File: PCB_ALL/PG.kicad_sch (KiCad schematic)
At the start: 25 parts, among them SW1 SW_SP3T, U4 NE555P

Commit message: Updated KiCAD project files
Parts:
- removed BT1: Battery_Cell, symbol Device:Battery_Cell
- removed SW1: SW_SP3T, symbol Switch:SW_SP3T
- added Ammeter+2, Ammeter+3, Ammeter-2, Ammeter-3, CAP3, CAP4, CAP5, CAP6, PWR+1, PWR-1, VBB3, VBB4, VBE+1, VBE-1, VCE+1, VCE-1, VDD1, VDD2, Vcc1, Vcc2, Vgg+2, Vgg-2: Conn_01x01, Connector_PinHeader_2.54mm:PinHeader_1x01_P2.54mm_Vertical, symbol Connector_Generic:Conn_01x01
- added Q4: NPN, symbol Simulation_SPICE:NPN
- added Q5: NMOS, symbol Simulation_SPICE:NMOS
- added R17, R18: R, symbol Device:R
- added R19: 100k, symbol Device:R
- added R20: 1k, symbol Device:R
- C5, C6, C7, C8: footprint (none) -> Capacitor_THT:C_Disc_D3.0mm_W2.0mm_P2.50mm
- CRO1, CRO2, SG1, SG2: footprint (none) -> Connector_PinHeader_2.54mm:PinHeader_1x01_P2.54mm_Vertical
- CRO3, CRO4: renamed from CRO; footprint (none) -> Connector_PinHeader_2.54mm:PinHeader_1x01_P2.54mm_Vertical
- D3: footprint (none) -> LED_THT:LED_D3.0mm
- D4: footprint (none) -> Diode_THT:D_A-405_P7.62mm_Horizontal
- L1: footprint (none) -> Inductor_THT:L_Axial_L5.3mm_D2.2mm_P7.62mm_Horizontal_Vishay_IM-1
- R13, R14, R15, R16, RV1: footprint (none) -> Resistor_THT:R_Axial_DIN0207_L6.3mm_D2.5mm_P7.62mm_Horizontal
- SG-1: renamed from SG-; footprint (none) -> Connector_PinHeader_2.54mm:PinHeader_1x01_P2.54mm_Vertical
- SQ+1: renamed from SQ+; footprint (none) -> Connector_PinHeader_2.54mm:PinHeader_1x01_P2.54mm_Vertical
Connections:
- net GND: now also Q5.3 (S), VDD2.1 (Pin_1), Vgg+2.1 (Pin_1)
- net at C7.1: now also CAP6.1 (Pin_1)
- net at CRO3.1 (Pin_1), L1.2: now also CAP3.1 (Pin_1)
- net at SQ+1.1 (Pin_1): now also PWR+1.1 (Pin_1)
- net at D4.2 (A): now also PWR-1.1 (Pin_1)
- net at C6.1: now also CAP5.1 (Pin_1)
- net at C5.1: now also CAP4.1 (Pin_1)
- new net: Q4.3 (E), VBB4.1 (Pin_1), VBE-1.1 (Pin_1), VCE-1.1 (Pin_1), Vcc2.1 (Pin_1)
- new net: Ammeter-2.1 (Pin_1), R17.2, VBE+1.1 (Pin_1)
- new net: R18.2, Vcc1.1 (Pin_1)
- new net: R20.2, VDD1.1 (Pin_1)
- new net: Ammeter+3.1 (Pin_1), R18.1, VCE+1.1 (Pin_1)
- new net: Q5.1 (D), R20.1
- new net: Q5.2 (G), R19.2
- new net: Ammeter-3.1 (Pin_1), Q4.1 (C)
- new net: Ammeter+2.1 (Pin_1), Q4.2 (B)
- new net: R19.1, Vgg-2.1 (Pin_1)
- new net: R17.1, VBB3.1 (Pin_1)
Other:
- note added: "CE"
- note added: "NMOS O/P and TRANSFER CHAR."
- note added: "To Do - PLL 565 Barrier Capacitance Delayed Linear Sweep"
- note removed: "To Do - PLL 565 Barrier Capacitance"
- moved on the sheet: C5, C6, C7, L1, R13

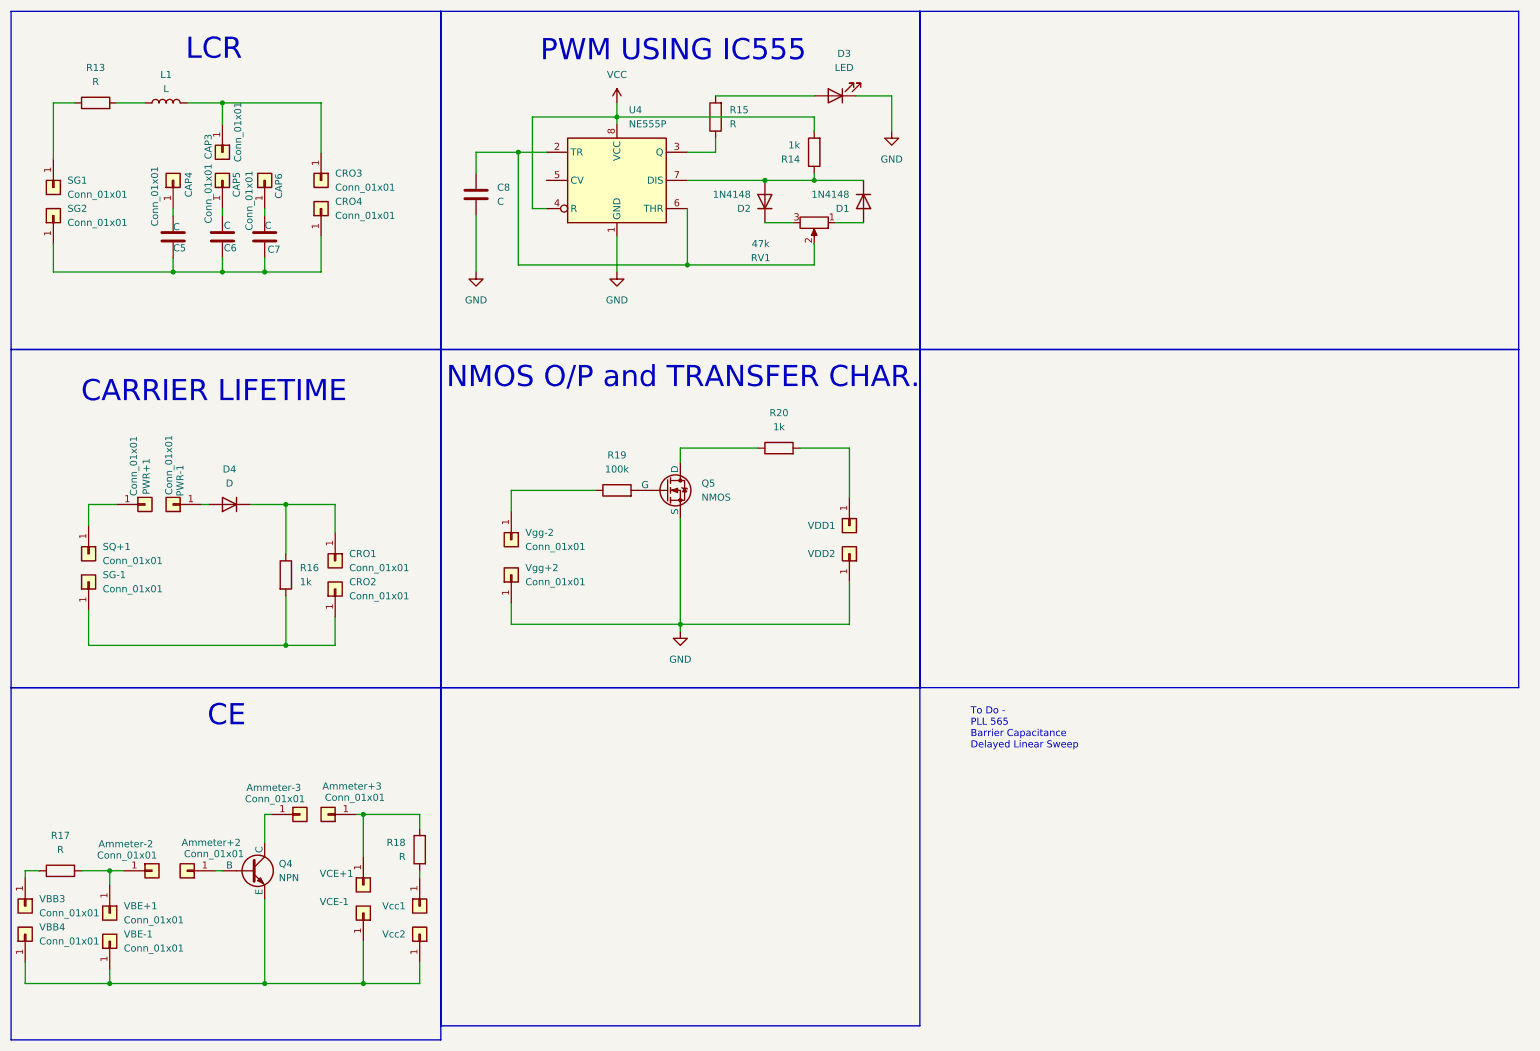
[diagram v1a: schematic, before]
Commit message: Updated KiCAD schematic and PCB layout
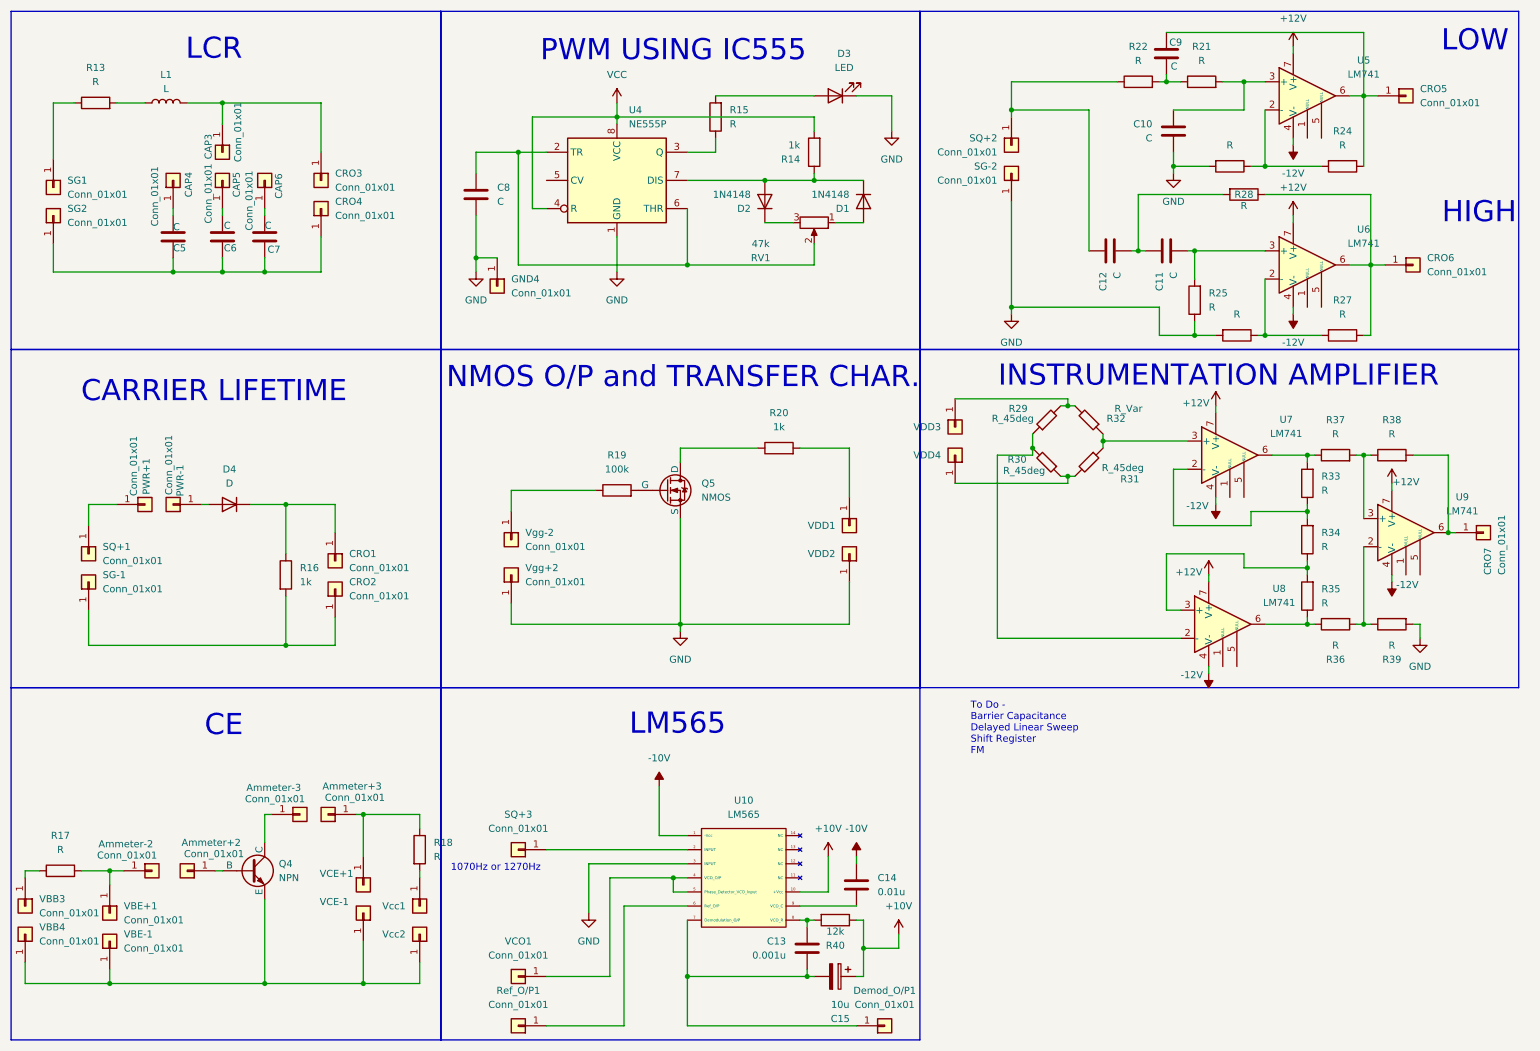
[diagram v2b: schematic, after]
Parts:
- added C10, C11, C12, C9: C, Capacitor_SMD:C_0805_2012Metric_Pad1.18x1.45mm_HandSolder, symbol Device:C
- added C13: 0.001u, Capacitor_SMD:C_0805_2012Metric_Pad1.18x1.45mm_HandSolder, symbol Device:C
- added C14: 0.01u, Capacitor_SMD:C_0805_2012Metric_Pad1.18x1.45mm_HandSolder, symbol Device:C
- added C15: 10u, Capacitor_THT:CP_Radial_D5.0mm_P2.50mm, symbol Device:C_Polarized
- added CRO5, CRO6, CRO7, Demod_O/P1, GND4, SG-2, SQ+2, SQ+3, VCO1, VDD3, VDD4: Conn_01x01, Connector_PinSocket_2.54mm:PinSocket_1x01_P2.54mm_Vertical, symbol Connector_Generic:Conn_01x01
- added R21, R22, R23, R24, R25, R26, R27, R28, R33, R34, R35, R36, R37, R38, R39: R, Resistor_SMD:R_0805_2012Metric_Pad1.20x1.40mm_HandSolder, symbol Device:R
- added R29, R30, R31: R_45deg, Resistor_SMD:R_0805_2012Metric_Pad1.20x1.40mm_HandSolder, symbol Device:R_45deg
- added R32: R_Var, Connector_PinSocket_2.54mm:PinSocket_2x01_P2.54mm_Vertical, symbol Device:R_45deg
- added R40: 12k, Resistor_SMD:R_0805_2012Metric_Pad1.20x1.40mm_HandSolder, symbol Device:R
- added Ref_O/P1: Conn_01x01, Connector_PinHeader_2.54mm:PinHeader_1x01_P2.54mm_Vertical, symbol Connector_Generic:Conn_01x01
- added U10: LM565, Package_DIP:CERDIP-14_W7.62mm_SideBrazed_LongPads, symbol W25Q64BVSSIG:LM565
- added U5, U6, U7, U8, U9: LM741, Package_SO:SOIC-8_3.9x4.9mm_P1.27mm, symbol Amplifier_Operational:LM741
- Ammeter+2, Ammeter+3, Ammeter-2, Ammeter-3, CAP3, CAP4, CAP5, CAP6, CRO1, CRO2, CRO3, CRO4, PWR+1, PWR-1, SG-1, SG1, SG2, SQ+1, VBB3, VBB4, VBE+1, VBE-1, VCE+1, VCE-1, VDD1, VDD2, Vcc1, Vcc2, Vgg+2, Vgg-2: footprint Connector_PinHeader_2.54mm:PinHeader_1x01_P2.54mm_Vertical -> Connector_PinSocket_2.54mm:PinSocket_1x01_P2.54mm_Vertical
- C5, C6, C7, C8: footprint Capacitor_THT:C_Disc_D3.0mm_W2.0mm_P2.50mm -> Capacitor_SMD:C_0805_2012Metric_Pad1.18x1.45mm_HandSolder
- Q4, Q5: footprint (none) -> Package_TO_SOT_SMD:SOT-23
- R13, R14, R15, R16: footprint Resistor_THT:R_Axial_DIN0207_L6.3mm_D2.5mm_P7.62mm_Horizontal -> Resistor_SMD:R_0805_2012Metric_Pad1.20x1.40mm_HandSolder
- R17, R18, R19, R20: footprint (none) -> Resistor_SMD:R_0805_2012Metric_Pad1.20x1.40mm_HandSolder
- RV1: footprint Resistor_THT:R_Axial_DIN0207_L6.3mm_D2.5mm_P7.62mm_Horizontal -> Potentiometer_THT:Potentiometer_Bourns_3296P_Horizontal
- U4: footprint Package_DIP:DIP-8_W7.62mm -> Package_SO:SOIC-8_3.9x4.9mm_P1.27mm
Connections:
- net GND: now also C10.2, GND4.1 (Pin_1), R23.2, R25.1, R26.2, R39.2, SG-2.1 (Pin_1), U10.3 (INPUT)
- new net: R37.2, R38.1, U9.3 (+)
- new net: CRO7.1 (Pin_1), R38.2, U9.6
- new net: C12.1, R22.1, SQ+2.1 (Pin_1)
- new net: C11.1, C12.2, R28.2
- new net: SQ+3.1 (Pin_1), U10.2 (INPUT)
- new net: R31.1, R32.1, U7.3 (+)
- new net: R30.1, R31.2, VDD4.1 (Pin_1)
- new net: C9.1, CRO5.1 (Pin_1), R24.1, U5.6
- new net: R36.2, R39.1, U9.2 (-)
- new net: R29.1, R30.2, U8.2 (-)
- new net: R29.2, R32.2, VDD3.1 (Pin_1)
- new net: CRO6.1 (Pin_1), R27.1, R28.1, U6.6
- new net: R26.1, R27.2, U6.2 (-)
- new net: R23.1, R24.2, U5.2 (-)
- new net: C10.1, R21.2, U5.3 (+)
- new net: C11.2, R25.2, U6.3 (+)
- new net: R33.1, R34.2, U7.2 (-)
- new net: R33.2, R37.1, U7.6
- new net: R34.1, R35.2, U8.3 (+)
- new net: R35.1, R36.1, U8.6
- new net: C9.2, R21.1, R22.2
- new net: C13.1, C15.2, Demod_O/P1.1 (Pin_1), U10.7 (Demodulation_O/P)
- new net: C14.1, U10.9 (VCO_C)
- new net: C13.2, R40.2, U10.8 (VCO_R)
- new net: U10.4 (VCO_O/P), U10.5 (Phase_Detector_VCO_Input), VCO1.1 (Pin_1)
- new net: Ref_O/P1.1 (Pin_1), U10.6 (Ref_O/P)
- new net +10V: C15.1, R40.1, U10.10 (+Vcc)
- new net +12V: U5.7 (V+), U6.7 (V+), U7.7 (V+), U8.7 (V+), U9.7 (V+)
- new net -10V: C14.2, U10.1 (-Vcc)
- new net -12V: U5.4 (V-), U6.4 (V-), U7.4 (V-), U8.4 (V-), U9.4 (V-)
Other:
- note added: "1070Hz or 1270Hz"
- note added: "HIGH"
- note added: "INSTRUMENTATION AMPLIFIER"
- note added: "LM565"
- note added: "LOW"
- note added: "To Do - Barrier Capacitance Delayed Linear Sweep Shift Register FM"
- note removed: "To Do - PLL 565 Barrier Capacitance Delayed Linear Sweep"
